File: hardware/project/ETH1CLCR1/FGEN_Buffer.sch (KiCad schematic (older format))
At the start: 60 parts, among them K701 9012, K702 9012, K703 9012, K704 9012, Q701 BC847W, Q702 BC847W, Q703 BC847W, Q704 BC847W, Q705 MMBT4401L, Q706 MMBT4403L, U701 LT1468, U702 TL072, U703 AQY212GS, U704 AD5293BRUZ-20

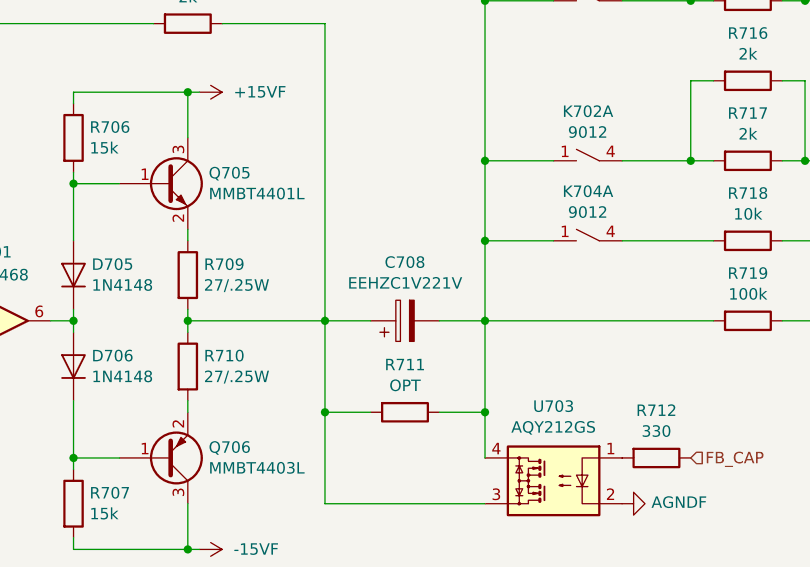
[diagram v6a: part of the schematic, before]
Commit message: Fixed some mistakes in the foorpeints. BOM list ready.
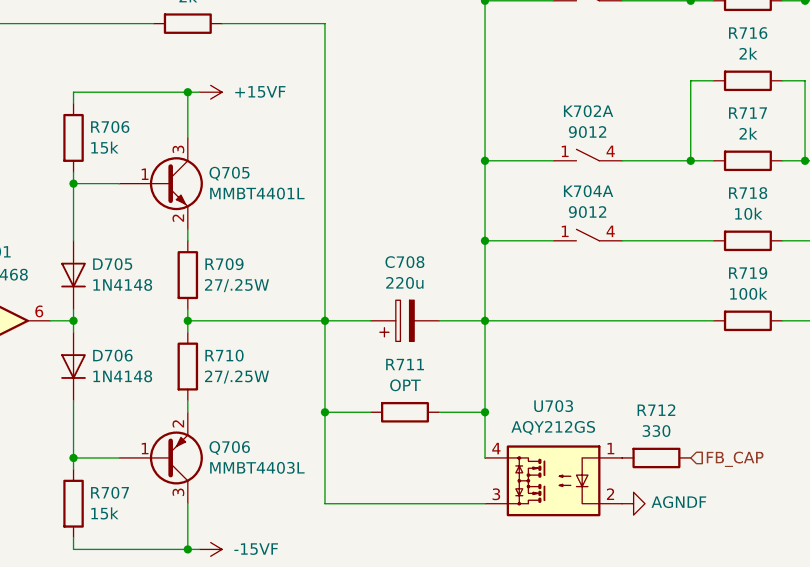
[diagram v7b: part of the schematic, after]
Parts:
- C708: value EEHZC1V221V -> 220u
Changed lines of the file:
@@
 P 5050 3200
 F 0 "C708" V 5305 3200 50  0000 C CNN
-F 1 " EEHZC1V221V" V 5214 3200 50  0000 C CNN
+F 1 "220u" V 5214 3200 50  0000 C CNN
 F 2 "Capacitor_SMD:CP_Elec_10x10" H 5088 3050 50  0001 C CNN
 F 3 "~" H 5050 3200 50  0001 C CNN

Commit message: PCB layout
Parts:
- added C715, C716: 10u/35V, Capacitor_SMD:C_1206_3216Metric_Pad1.42x1.75mm_HandSolder, symbol Device:C
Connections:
- net +15VF: now also C715.1
- net -15VF: now also C716.1
- net AGNDF: now also C715.2, C716.2
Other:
- moved on the sheet: C701, C702, C703, C704, C708, C713, D701, D702, D703, D704, D705, D706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
